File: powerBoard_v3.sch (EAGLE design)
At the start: 25 parts, among them U1 TLE2426CD

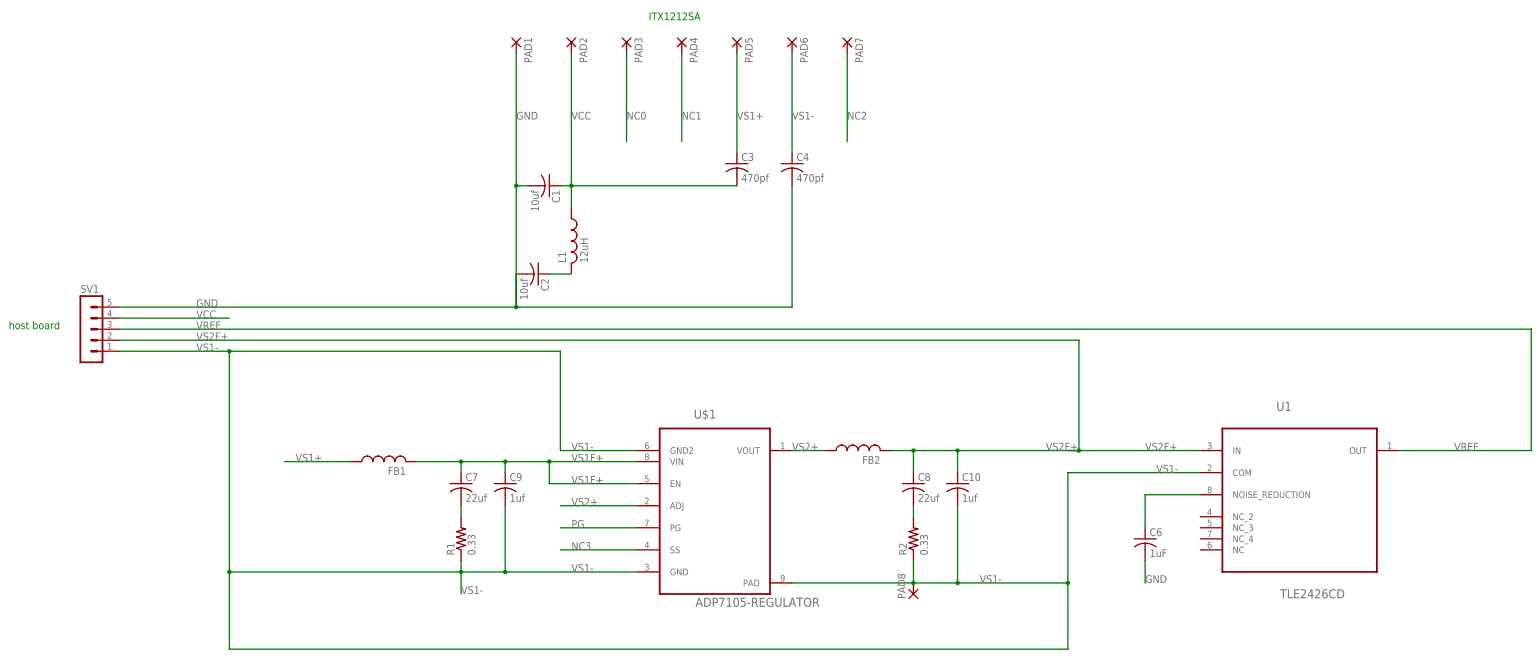
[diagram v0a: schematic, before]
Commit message: updated power board designs: v2 uses low current 2.5v reference, v3 uses 10v rail and 5v ref both with simple linear regulators. Added breakout board to go from DB37 to BNC
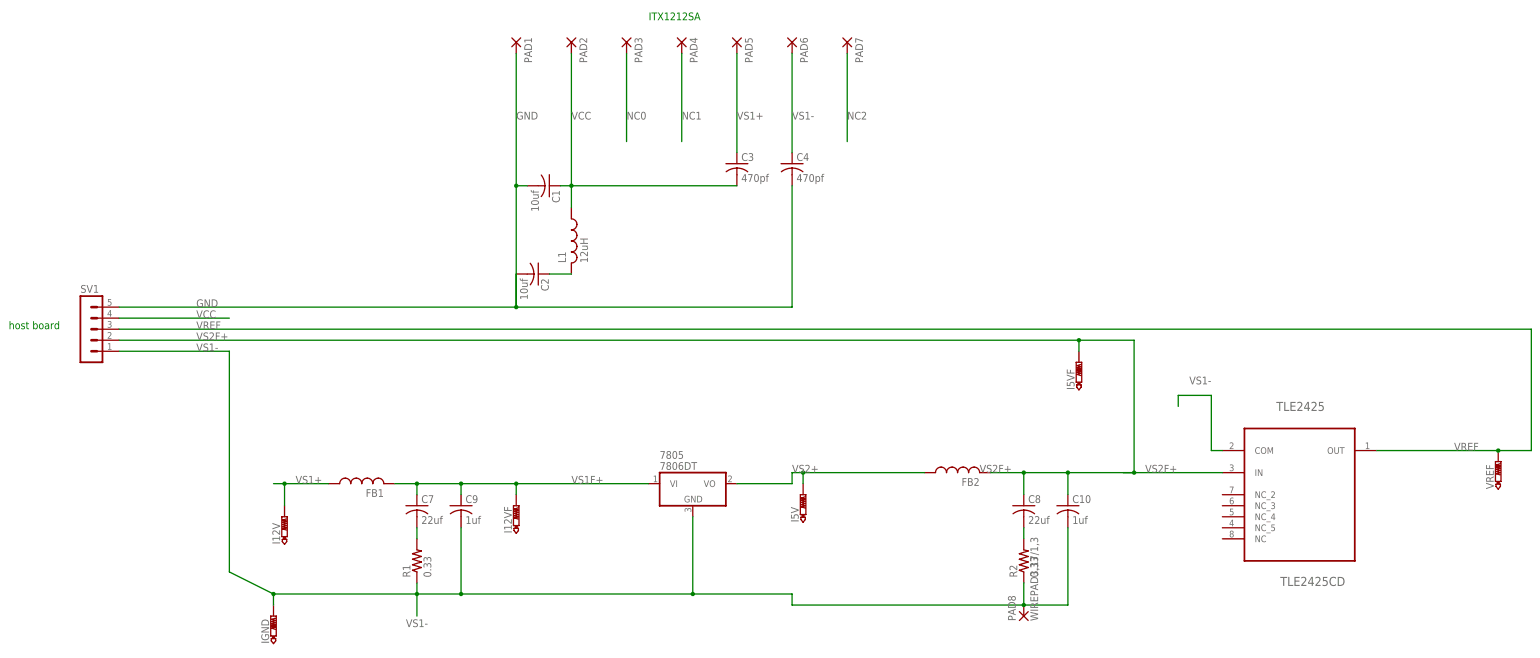
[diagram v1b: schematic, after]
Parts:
- removed C6: 1uF, rcl:C-USC0805
- removed U$1: ADP7105-REGULATOR, tuckerLib:ADP7105-REGULATOR
- removed U1: TLE2426CD, Texas Instruments_By_element14_Batch_1:TLE2426CD
- added 7805: 7806DT, linear:7806DT
- added I12V, I12VF, I5V, I5VF, IGND, VREF: PTR1PAD1-13, testpad:PTR1PAD1-13
- added TLE2425: TLE2425CD, Texas Instruments_By_element14_Batch_1:TLE2425CD
- PAD8: value (none) -> WIREPAD3,17/1,3; device wirepad:2,54/1,1 -> wirepad:WIREPAD3,17/1,3
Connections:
- removed net N$2: C6.1, U1.NOISE_REDUCTION
- removed net NC3: U$1.SS
- removed net PG: U$1.PG
- net GND: no longer C6.2
- net VREF: now also TLE2425.OUT, VREF.TP; no longer U1.OUT
- net VS1+: now also I12V.TP
- net VS1-: now also 7805.GND, IGND.TP, TLE2425.COM; no longer U$1.GND, U$1.GND2, U$1.PAD, U1.COM
- net VS1F+: now also 7805.VI, I12VF.TP; no longer U$1.EN, U$1.VIN
- net VS2+: now also 7805.VO, I5V.TP; no longer U$1.ADJ, U$1.VOUT
- net VS2F+: now also I5VF.TP, TLE2425.IN; no longer U1.IN
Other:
- moved on the sheet: C10, C7, C8, C9, FB1, FB2, R1, R2
